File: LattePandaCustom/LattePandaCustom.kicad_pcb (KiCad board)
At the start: 4 copper layers, 164.2 x 98.9 mm, 233 parts, among them J1 Conn_01x03_Pin, J10 Conn_01x03_Pin, J11 Conn_01x03_Pin, J12 Conn_01x04_Pin, J13 Conn_01x04_Pin, J14 Conn_01x03_Pin, J15 Bus_M.2_Socket_M, J16 Bus_M.2_Socket_E, J17 Barrel_Jack_Switch, J18 USB_C_Receptacle_USB2.0_16P, J19 Conn_01x04_Pin, J20 Conn_01x04_Pin, J21 Conn_01x04_Pin, J3 HDMI_A, J4 USB3_A_Stacked, J5 USB_A_Stacked, J6 RJ45_RB1-125B8G1A, J7 Conn_01x04_Pin, J8 Conn_01x03_Pin, J9 Conn_01x04_Pin, M1 Fan_4pin, Q1 2N7002, Q2 2SK3018, Q3 2SK3018, Q4 2SK3018, Q8 2N7002, SW1 SW_Push, SW2 SW_Push, U1 TPAZ1O23-04F, U10 ULC0524, U11 ULC0524, U12 ULC0524, U14 USB PD等快充协议受电芯片-CH224K-ESSOP10, U15 LM2734X, U16 LM2734X, U17 ULC0524, U2 TPAZ1O23-04F, U3 ULC0524, U4 ULC0524, U5 ULC0524, U6 RTL8111H-CG-RH, U7 ULC0524, U8 ULC0524, U9 ULC0524, Y1 25MHz

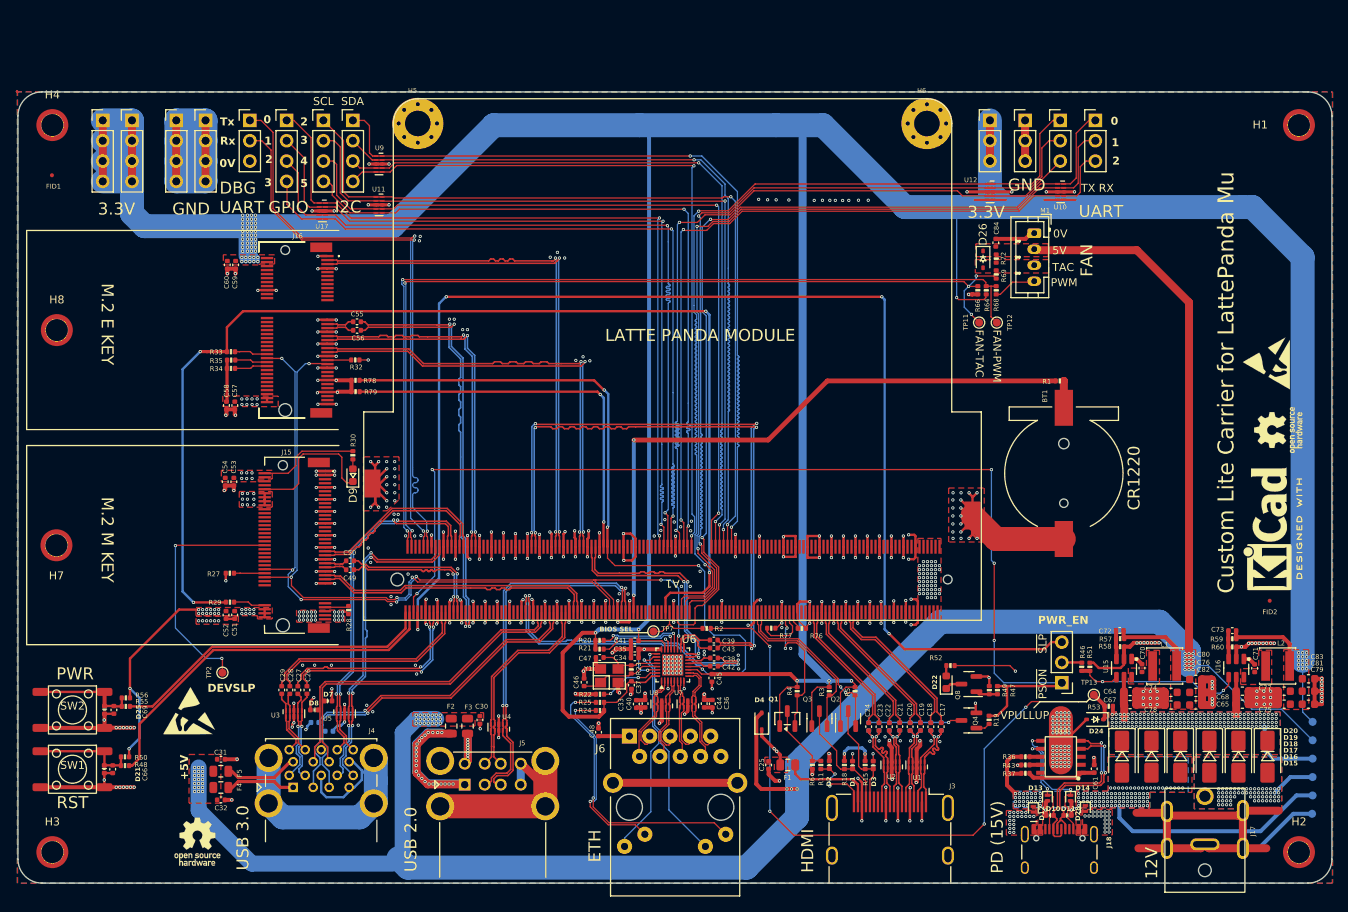
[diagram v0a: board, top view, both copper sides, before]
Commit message: added GND stitching vias to PCB and added 3D renders and PCB images
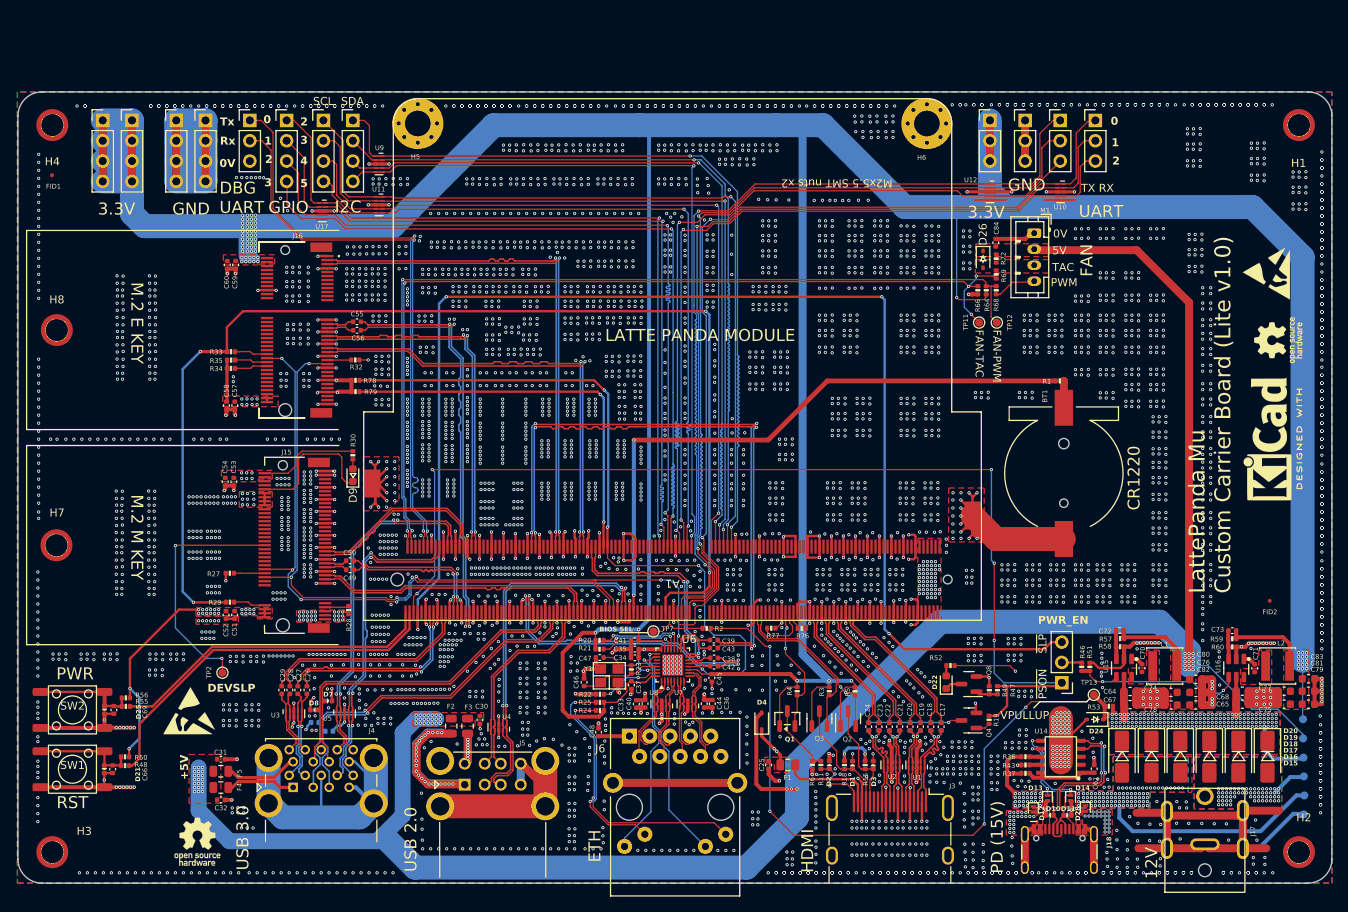
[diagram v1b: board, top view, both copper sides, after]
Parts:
- moved REF** 11.2 mm to (222.5, 101.8)
- moved REF** 11.2 mm to (222.3, 81.1)
- moved REF** 11.2 mm to (223.9, 89.4)
- moved TP6 1.24 mm to (226.9, 136.8)
- moved TP5 1.22 mm to (226.9, 139.2)
- moved TP10 1.15 mm to (227.0, 141.6)
- moved TP4 1.10 mm to (227.1, 143.9)
- moved TP3 1.04 mm to (227.1, 146.3)
- moved TP15 1.04 mm to (227.1, 148.7)
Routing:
- net GND: track 722.9 -> 733.9 mm, vias 549 -> 4931
- net +5V: track 284.4 -> 280.7 mm
- net /HDMI/DDI_B_HPD: track 18.3 -> 16.2 mm
- net +1V0: track 29.1 -> 31.1 mm
- net VDC: track 98.8 -> 97.7 mm
- net +12V: track 5.56 -> 4.50 mm
- net +15V: track 36.5 -> 35.5 mm, vias 115 -> 113
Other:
- board text added: "LattePanda Mu Custom Carrier Board (Lite v1.0)"
- board text removed: "Custom Lite Carrier for LattePanda Mu"
